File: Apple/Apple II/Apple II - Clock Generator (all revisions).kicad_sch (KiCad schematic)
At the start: 24 parts, among them Q1 2N4258, Q2 2N4258, Y1 14.318MHz

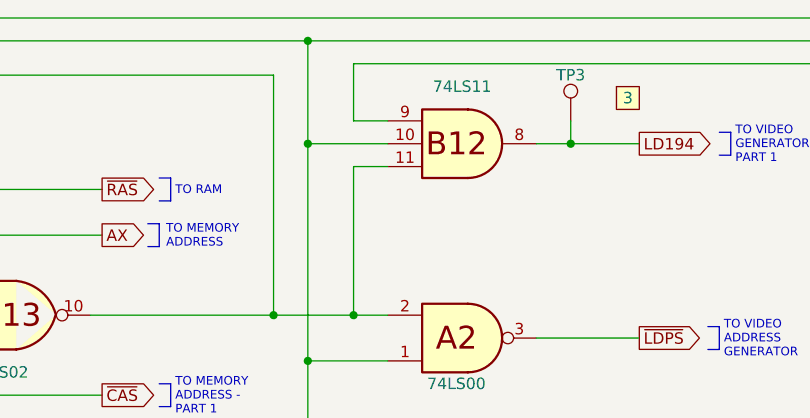
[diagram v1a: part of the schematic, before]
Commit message: Finished Apple II - Sheet 16 - Video Generator Part 1 (Rev 7, RFI)
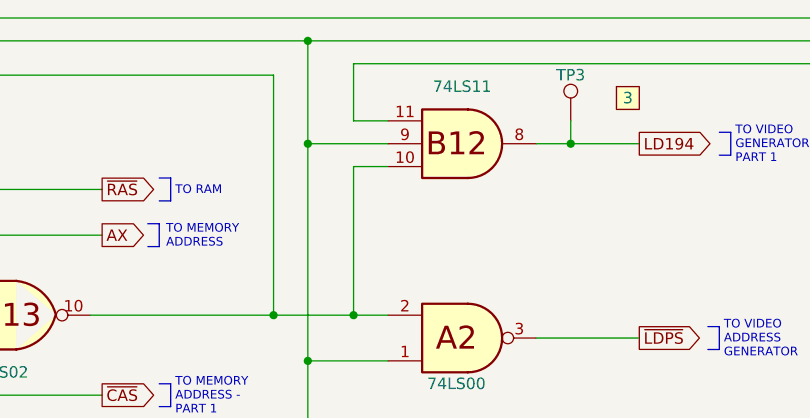
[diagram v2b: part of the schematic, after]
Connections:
- net ~{7M}: now also B12.11; no longer B12.9
- net ɸ0_{40}: now also B12.9; no longer B12.10
- net at A2.2, B13.10, D2.5: now also B12.10; no longer B12.11

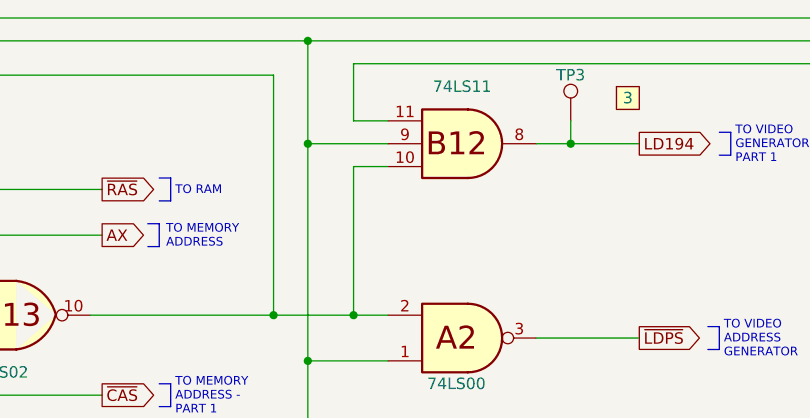
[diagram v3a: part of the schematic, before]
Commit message: Finished Apple II - Single Piece Keyboard
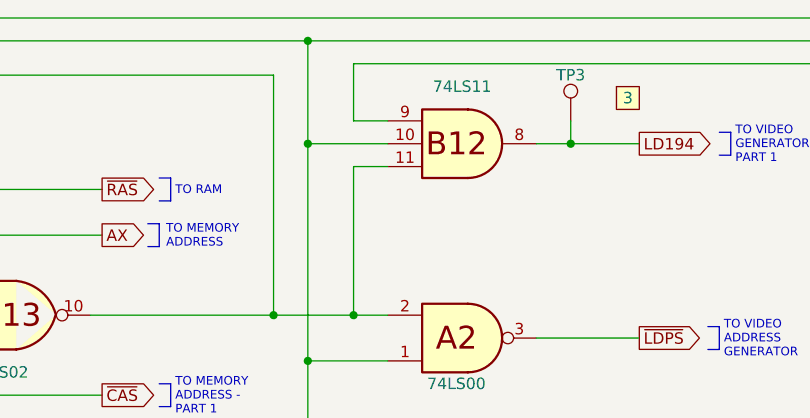
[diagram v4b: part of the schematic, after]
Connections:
- net ~{7M}: now also B12.9; no longer B12.11
- net ɸ0_{40}: now also B12.10; no longer B12.9
- net at A2.2, B13.10, D2.5: now also B12.11; no longer B12.10
